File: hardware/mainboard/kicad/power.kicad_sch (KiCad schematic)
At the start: 38 parts, among them J1 1S LiPo PCM / PH-2, J8 External cell NTC / hand sold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, Q2 AO3401A, SW1 MK-12C03-G015, U3 BQ24072TRGTR, U4 TPS63802DLAR

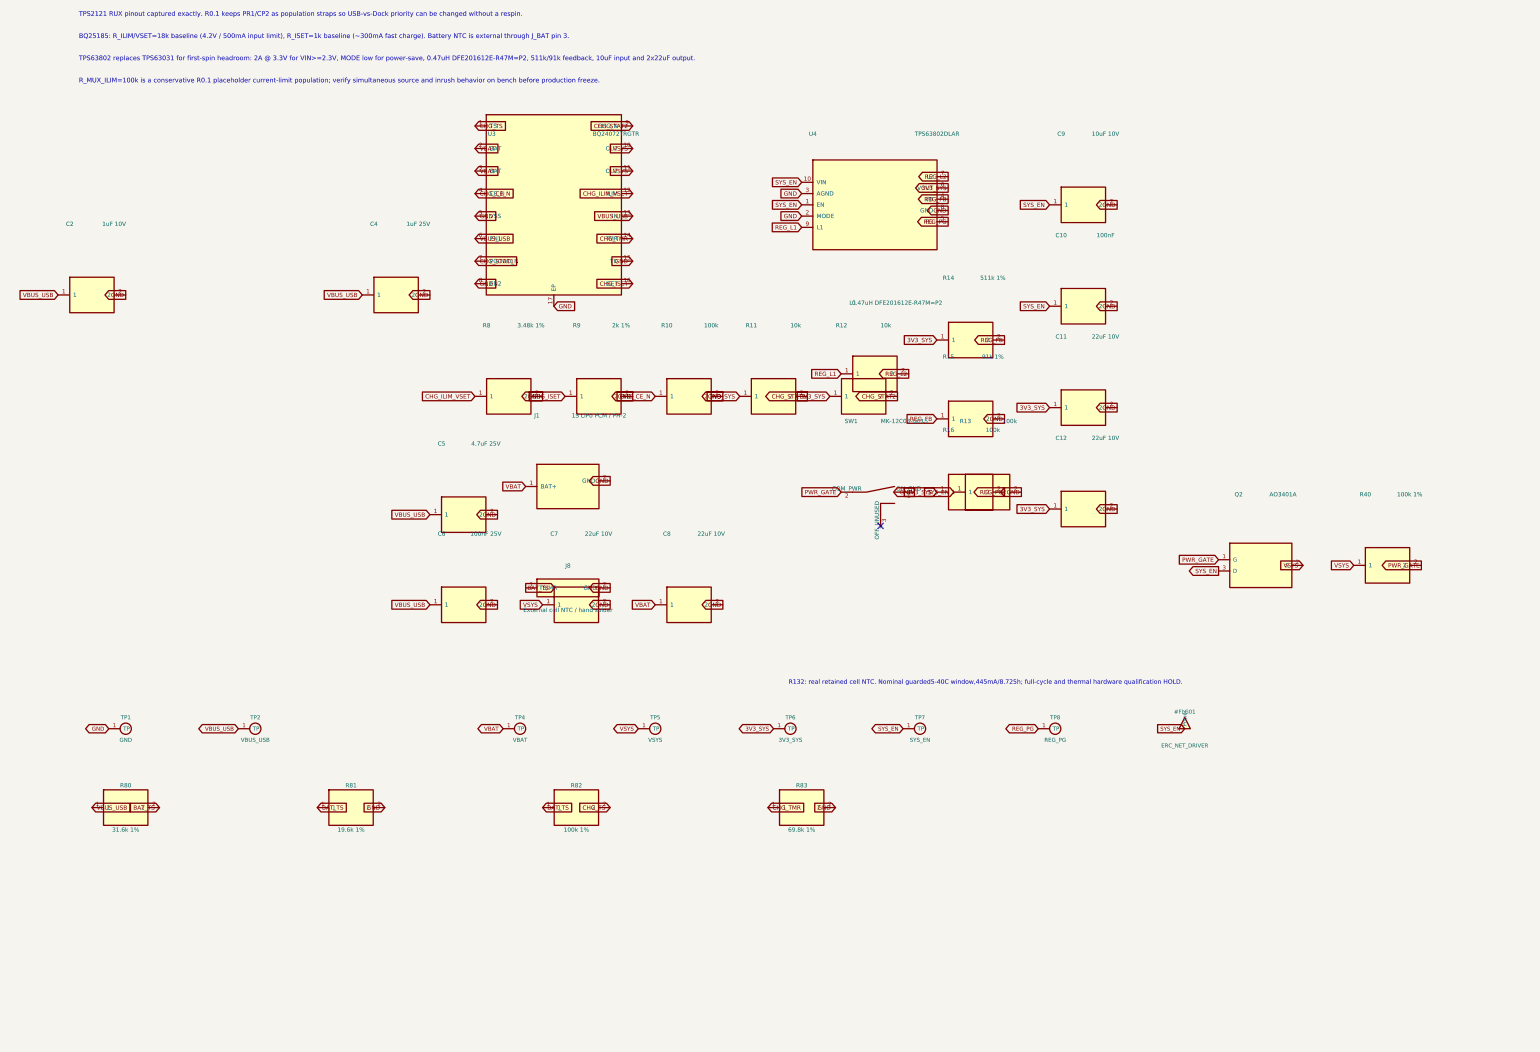
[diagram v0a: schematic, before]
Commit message: R132: close voltage-TS charger, preserve USB reference, thin-pack supply and native guards; NO FAB
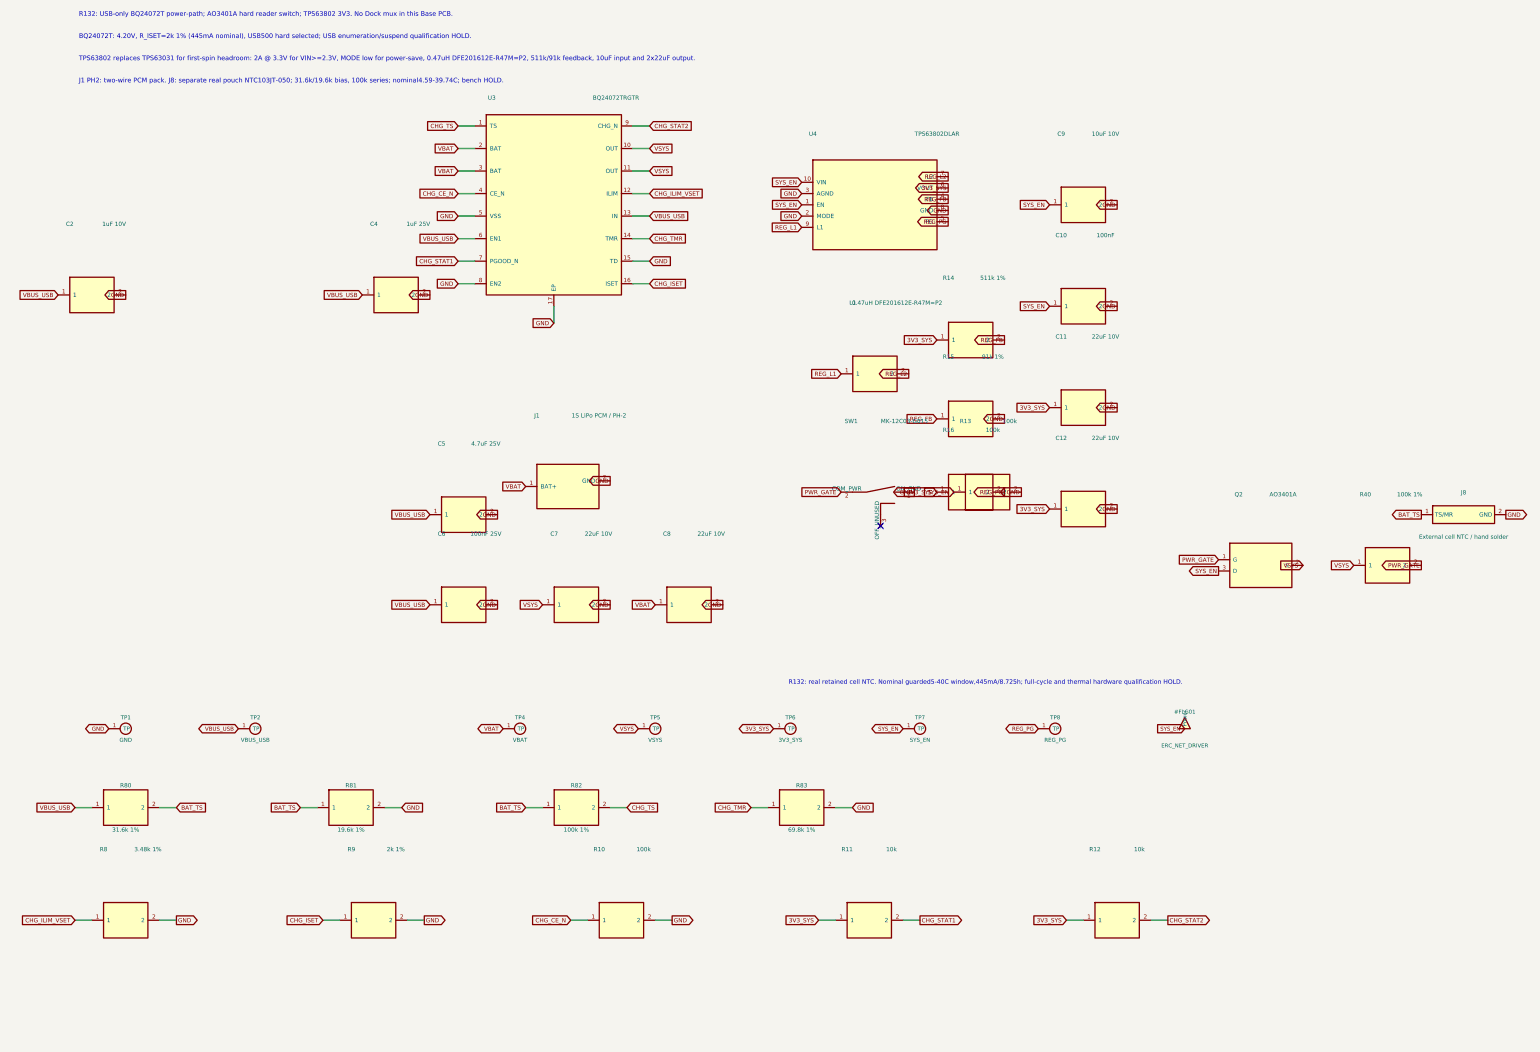
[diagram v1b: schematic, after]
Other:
- note added: "BQ24072T: 4.20V, R_ISET=2k 1% (445mA nominal), USB500 hard selected; USB enumeration/suspend qualification HOLD."
- note added: "J1 PH2: two-wire PCM pack. J8: separate real pouch NTC103JT-050; 31.6k/19.6k bias, 100k series; nominal4.59-39.74C; bench HOLD."
- note added: "R132: USB-only BQ24072T power-path; AO3401A hard reader switch; TPS63802 3V3. No Dock mux in this Base PCB."
- note removed: "BQ25185: R_ILIM/VSET=18k baseline (4.2V / 500mA input limit), R_ISET=1k baseline (~300mA fast charge). Battery NTC is external through J_BAT pin 3."
- note removed: "R_MUX_ILIM=100k is a conservative R0.1 placeholder current-limit population; verify simultaneous source and inrush behavior on bench before production freeze."
- note removed: "TPS2121 RUX pinout captured exactly. R0.1 keeps PR1/CP2 as population straps so USB-vs-Dock priority can be changed without a respin."
- title: ENKU R0.1 — Power -> ENKU Base — Power
- moved on the sheet: J8, R10, R11, R12, R8, R9

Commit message: R134 working checkpoint: real USB4215 replacement and GPIO charger control; ten routes pending, NO FAB
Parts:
- added R84, R85: 2.2k 1%, ENKU:R_RC0603_YAGEO_REFLOW, symbol ENKU:R
- added R86, R87, R88: 1k 1%, ENKU:R_RC0603_YAGEO_REFLOW, symbol ENKU:R
- U3: Charge Profile R132 445mA nominal; USB500 max500mA; voltage-TS guarded win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 -> R134 GPIO16/2 EN1/EN2;GPIO38 CE;reset/OFF high-Z USB100;aut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
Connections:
- net CHG_CE_N: now also R88.2
- net GND: now also R84.2, R85.2; no longer U3.5 (VSS)
- net VBUS_USB: no longer U3.6 (EN1)
- new net CHG_CE_CMD: R88.1
- new net CHG_EN1: R84.1, R86.2, U3.6 (EN1)
- new net CHG_EN1_CMD: R86.1
- new net CHG_EN2: R85.1, R87.2, U3.5 (EN2)
- new net CHG_EN2_CMD: R87.1

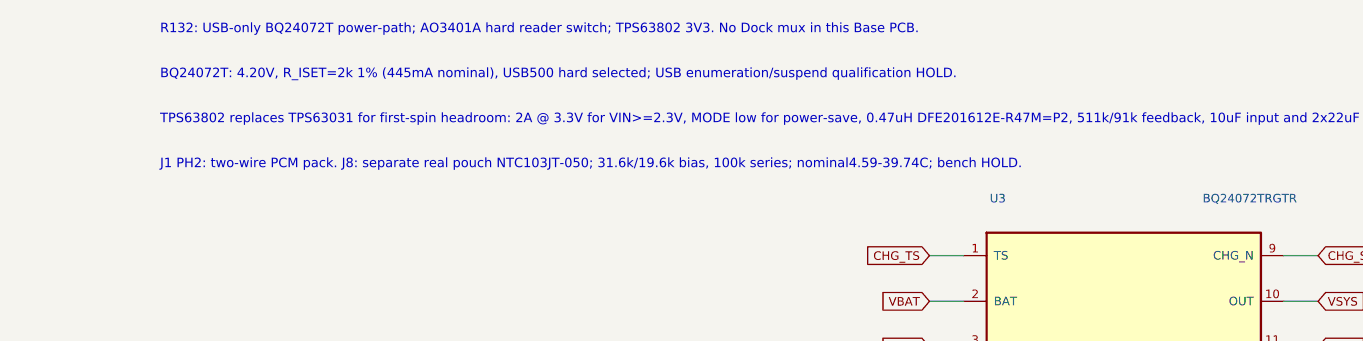
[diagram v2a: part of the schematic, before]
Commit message: Close R134 native routing at unchanged0.20mm minimum; retain16 button findings, NO FAB
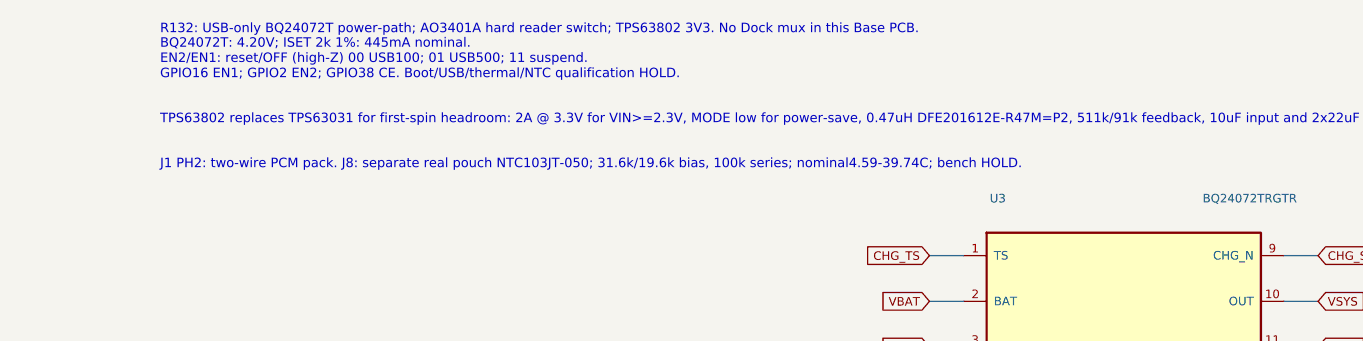
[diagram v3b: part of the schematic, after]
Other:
- note added: "BQ24072T: 4.20V; ISET 2k 1%: 445mA nominal. EN2/EN1: reset/OFF (high-Z) 00 USB100; 01 USB500; 11 suspend. GPIO16 EN1; GPIO2 EN2; GPIO38 CE. Boot/USB/thermal/NTC qualification HOLD."
- note removed: "BQ24072T: 4.20V, R_ISET=2k 1% (445mA nominal), USB500 hard selected; USB enumeration/suspend qualification HOLD."
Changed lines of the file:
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@@
 	(global_label "REG_PG" (shape output) (at 233.68 127 180) (effects (font (size 0.95 0.95)) (justify right bottom)))
 	(text "R132: USB-only BQ24072T power-path; AO3401A hard reader switch; TPS63802 3V3. No Dock mux in this Base PCB." (exclude_from_sim no) (at 25 20 0) (effects (font (size 1.05 1.05)) (justify left bottom)))
-	(text "BQ24072T: 4.20V, R_ISET=2k 1% (445mA nominal), USB500 hard selected; USB enumeration/suspend qualification HOLD." (exclude_from_sim no) (at 25 25 0) (effects (font (size 1.05 1.05)) (justify left bottom)))
+	(text "BQ24072T: 4.20V; ISET 2k 1%: 445mA nominal.\nEN2/EN1: reset/OFF (high-Z) 00 USB100; 01 USB500; 11 suspend.\nGPIO16 EN1; GPIO2 EN2; GPIO38 CE. Boot/USB/thermal/NTC qualification HOLD." (exclude_from_sim no) (at 25 25 0) (effects (font (size 1.05 1.05)) (justify left bottom)))
 	(text "TPS63802 replaces TPS63031 for first-spin headroom: 2A @ 3.3V for VIN>=2.3V, MODE low for power-save, 0.47uH DFE201612E-R47M=P2, 511k/91k feedback, 10uF input and 2x22uF output." (exclude_from_sim no) (at 25 30 0) (effects (font (size 1.05 1.05)) (justify left bottom)))
 	(text "J1 PH2: two-wire PCM pack. J8: separate real pouch NTC103JT-050; 31.6k/19.6k bias, 100k series; nominal4.59-39.74C; bench HOLD." (exclude_from_sim no) (at 25 35 0) (effects (font (size 1.05 1.05)) (justify left bottom)))

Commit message: R135 native DRC/ERC/parity zero after genuine no-boss switches and TS bias correction; independent audits pending, NO FAB
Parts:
- R80: value 31.6k 1% -> 40.2k 1%; MPN RC0603FR-0731K6L -> RC0603FR-0740K2L
- R81: value 19.6k 1% -> 33.2k 1%; MPN RC0603FR-0719K6L -> RC0603FR-0733K2L
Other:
- note added: "J1 PH2: two-wire PCM pack. J8: separate real pouch NTC103JT-050; 40.2k/33.2k bias, 100k series; nominal4.90-35.01C; R81-open hot model inhibits; bench HOLD."
- note added: "R135: real retained cell NTC. Conservative nominal4.90-35.01C window,445mA/8.725h; full-cycle and thermal hardware qualification HOLD."
- note removed: "J1 PH2: two-wire PCM pack. J8: separate real pouch NTC103JT-050; 31.6k/19.6k bias, 100k series; nominal4.59-39.74C; bench HOLD."
- note removed: "R132: real retained cell NTC. Nominal guarded5-40C window,445mA/8.725h; full-cycle and thermal hardware qualification HOLD."
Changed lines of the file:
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@@
 	(generator_version "8.0")
 	(paper "A3")
-	(title_block (title "ENKU Base — Power") (date "2026-10-11") (rev "R134 NO FAB") (company "ENKU") (comment 1 "BQ24072T PH2 battery + separate cell NTC + switched 3V3"))
+	(title_block (title "ENKU Base — Power") (date "2026-10-11") (rev "R135 NO FAB") (company "ENKU") (comment 1 "BQ24072T PH2 battery + separate cell NTC + switched 3V3"))
 	(symbol (lib_id "ENKU:BQ24072T_RGT") (at 132.08 62.23 0) (unit 1) (exclude_from_sim no) (in_bom yes) (on_board yes) (dnp no)
 		(property "Reference" "U3" (at 118.08 38.1 0) (effects (font (size 0.95 0.95))))
@@
 	(text "BQ24072T: 4.20V; ISET 2k 1%: 445mA nominal.\nEN2/EN1: reset/OFF (high-Z) 00 USB100; 01 USB500; 11 suspend.\nGPIO16 EN1; GPIO2 EN2; GPIO38 CE. Boot/USB/thermal/NTC qualification HOLD." (exclude_from_sim no) (at 25 25 0) (effects (font (size 1.05 1.05)) (justify left bottom)))
 	(text "TPS63802 replaces TPS63031 for first-spin headroom: 2A @ 3.3V for VIN>=2.3V, MODE low for power-save, 0.47uH DFE201612E-R47M=P2, 511k/91k feedback, 10uF input and 2x22uF output." (exclude_from_sim no) (at 25 30 0) (effects (font (size 1.05 1.05)) (justify left bottom)))
-	(text "J1 PH2: two-wire PCM pack. J8: separate real pouch NTC103JT-050; 31.6k/19.6k bias, 100k series; nominal4.59-39.74C; bench HOLD." (exclude_from_sim no) (at 25 35 0) (effects (font (size 1.05 1.05)) (justify left bottom)))
+	(text "J1 PH2: two-wire PCM pack. J8: separate real pouch NTC103JT-050; 40.2k/33.2k bias, 100k series; nominal4.90-35.01C; R81-open hot model inhibits; bench HOLD." (exclude_from_sim no) (at 25 35 0) (effects (font (size 1.05 1.05)) (justify left bottom)))
 	(symbol (lib_id "ENKU:TESTPOINT") (at 35.56 180.34 0) (unit 1) (exclude_from_sim no) (in_bom no) (on_board yes) (dnp no)
 		(property "Reference" "TP1" (at 35.56 177.8 0) (effects (font (size 0.9 0.9))))
@@
    (global_label "BAT_TS" (shape output) (at 327.66 132.08 0) (effects (font (size .95 .95)) (justify right bottom)))
    (global_label "GND" (shape output) (at 346.71 132.08 180) (effects (font (size .95 .95)) (justify left bottom)))
-   (text "R132: real retained cell NTC. Nominal guarded5-40C window,445mA/8.725h; full-cycle and thermal hardware qualification HOLD." (at 185 170 0) (effects (font (size 1 1)) (justify left)))
+   (text "R135: real retained cell NTC. Conservative nominal4.90-35.01C window,445mA/8.725h; full-cycle and thermal hardware qualification HOLD." (at 185 170 0) (effects (font (size 1 1)) (justify left)))
 (global_label "CHG_TS" (shape input) (at 110.49 44.45 0) (effects (font (size .95 .95)) (justify right bottom)))
 (global_label "VBAT" (shape input) (at 110.49 49.53 0) (effects (font (size .95 .95)) (justify right bottom)))
@@
 (symbol (lib_id "ENKU:R") (at 35.56 198.12 0) (unit 1) (exclude_from_sim no) (in_bom yes) (on_board yes) (dnp no)
 		(property "Reference" "R80" (at 35.56 193.12 0) (effects (font (size 0.95 0.95))))
-		(property "Value" "31.6k 1%" (at 35.56 203.12 0) (effects (font (size 0.95 0.95))))
+		(property "Value" "40.2k 1%" (at 35.56 203.12 0) (effects (font (size 0.95 0.95))))
 		(property "Footprint" "ENKU:R_RC0603_YAGEO_REFLOW" (at 142.24 105.41 0) (effects (font (size 0.95 0.95)) (hide yes)))
 		(property "Datasheet" "https://yageogroup.com/content/datasheet/asset/file/PYU-RC_GROUP_51_ROHS_L" (at 142.24 105.41 0) (effects (font (size 0.95 0.95)) (hide yes)))
-		(property "Description" "31.6k 1% R132 charger network" (at 142.24 105.41 0) (effects (font (size 0.95 0.95)) (hide yes)))
+		(property "Description" "R135 TS bias; bounded R81-open hot-inhibit model; leakage/attachment bench HOLD" (at 142.24 105.41 0) (effects (font (size 0.95 0.95)) (hide yes)))
 		(pin "1")
 		(pin "2")
 		(instances (project "enku-mainboard-r0.1" (path "/10000000-0000-4000-8000-000000000001/9b32661d-bae0-4f6c-b297-d680f24b8103" (reference "R80") (unit 1))))
-		(property "MPN" "RC0603FR-0731K6L" (at 0 0 0) (effects (font (size .8 .8)) (hide yes)))
+		(property "MPN" "RC0603FR-0740K2L" (at 0 0 0) (effects (font (size .8 .8)) (hide yes)))
 		(property "Manufacturer" "Yageo" (at 0 0 0) (effects (font (size .8 .8)) (hide yes)))
 		(property "Assembly" "FIT" (at 0 0 0) (effects (font (size .8 .8)) (hide yes)))
@@
 (symbol (lib_id "ENKU:R") (at 86.36 198.12 0) (unit 1) (exclude_from_sim no) (in_bom yes) (on_board yes) (dnp no)
 		(property "Reference" "R81" (at 86.36 193.12 0) (effects (font (size 0.95 0.95))))
-		(property "Value" "19.6k 1%" (at 86.36 203.12 0) (effects (font (size 0.95 0.95))))
+		(property "Value" "33.2k 1%" (at 86.36 203.12 0) (effects (font (size 0.95 0.95))))
 		(property "Footprint" "ENKU:R_RC0603_YAGEO_REFLOW" (at 142.24 105.41 0) (effects (font (size 0.95 0.95)) (hide yes)))
 		(property "Datasheet" "https://yageogroup.com/content/datasheet/asset/file/PYU-RC_GROUP_51_ROHS_L" (at 142.24 105.41 0) (effects (font (size 0.95 0.95)) (hide yes)))
-		(property "Description" "19.6k 1% R132 charger network" (at 142.24 105.41 0) (effects (font (size 0.95 0.95)) (hide yes)))
+		(property "Description" "R135 TS bias; bounded R81-open hot-inhibit model; leakage/attachment bench HOLD" (at 142.24 105.41 0) (effects (font (size 0.95 0.95)) (hide yes)))
 		(pin "1")
 		(pin "2")
 		(instances (project "enku-mainboard-r0.1" (path "/10000000-0000-4000-8000-000000000001/99e5236f-ad5a-4300-8efc-ae10e6f923e9" (reference "R81") (unit 1))))
-		(property "MPN" "RC0603FR-0719K6L" (at 0 0 0) (effects (font (size .8 .8)) (hide yes)))
-		(property "Manufacturer" "Yageo" (at 0 0 0) (effects (font (size .8 .8)) (hide yes)))
-		(property "Assembly" "FIT" (at 0 0 0) (effects (font (size .8 .8)) (hide yes)))
+		(property "MPN" "RC0603FR-0733K2L" (at 0 0 0) (effects (font (size .8 .8)) (hide yes)))
+		(property "Manufacturer" "Yageo" (at 0 0 0) (effects (font (size .8 .8)) (hide yes)))
+		(property "Assembly" "FIT" (at 0 0 0) (effects (font (size .8 .8)) (hide yes)))
